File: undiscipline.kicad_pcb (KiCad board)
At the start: 2 copper layers, 243 parts, among them J1 Conn_01x04_Male, J2 AVR-ISP-6, J2 USB_B_Micro, SW1 SW_Push, SW10 SW_Push, SW11 SW_Push, SW12 SW_Push, SW13 SW_Push, SW14 SW_Push, SW15 SW_Push, SW16 SW_Push, SW17 SW_Push, SW18 SW_Push, SW19 SW_Push, SW2 SW_Push, SW20 SW_Push, SW21 SW_Push, SW22 SW_Push, SW23 SW_Push, SW24 SW_Push, SW25 SW_Push, SW26 SW_Push, SW27 SW_Push, SW28 SW_Push, SW29 SW_Push, SW3 SW_Push, SW30 SW_Push, SW31 SW_Push, SW32 SW_Push, SW33 SW_Push, SW34 SW_Push, SW35 SW_Push, SW36 SW_Push, SW37 SW_Push, SW38 SW_Push, SW39 SW_Push, SW4 SW_Push, SW40 SW_Push, SW41 SW_Push, SW42 SW_Push, SW43 SW_Push, SW44 SW_Push, SW45 SW_Push, SW46 SW_Push, SW47 SW_Push, SW48 SW_Push, SW49 SW_Push, SW5 SW_Push, SW50 SW_Push, SW51 SW_Push, SW52 SW_Push, SW53 SW_Push, SW54 SW_Push, SW55 SW_Push, SW56 SW_Push, SW57 SW_Push, SW58 SW_Push, SW59 SW_Push, SW6 SW_Push, SW60 SW_Push, SW61 SW_Push, SW62 SW_Push, SW63 SW_Push, SW64 SW_Push, SW65 SW_Push, SW66 SW_Push, SW67 SW_Push, SW68 SW_Push, SW69 SW_Push, SW7 SW_Push, SW70 SW_Push, SW71 SW_Push, SW72 SW_Push, SW73 SW_Push, SW74 SW_Push, SW75 SW_Push, SW8 SW_Push, SW9 SW_Push, U1 ATmega32A-PU, Y1 16MHz

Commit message: Add ws2812b footprint
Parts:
- moved REF** 0.18 mm to (52.2, 80.9)

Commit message: Add LEDs under each key
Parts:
- removed the REF** at (52.2, 80.9)
- added D100: WS2812B, LED_SMD:LED_WS2812B_PLCC4_5.0x5.0mm_P3.2mm, F.Cu at (80.5, 123.7)
- added D101: WS2812B, LED_SMD:LED_WS2812B_PLCC4_5.0x5.0mm_P3.2mm, F.Cu at (99.5, 123.7)
- added D102: WS2812B, LED_SMD:LED_WS2812B_PLCC4_5.0x5.0mm_P3.2mm, F.Cu at (118.5, 123.7)
- added D103: WS2812B, LED_SMD:LED_WS2812B_PLCC4_5.0x5.0mm_P3.2mm, F.Cu at (137.5, 123.7)
- added D104: WS2812B, LED_SMD:LED_WS2812B_PLCC4_5.0x5.0mm_P3.2mm, F.Cu at (156.5, 123.7)
- added D105: WS2812B, LED_SMD:LED_WS2812B_PLCC4_5.0x5.0mm_P3.2mm, F.Cu at (175.5, 123.7)
- added D106: WS2812B, LED_SMD:LED_WS2812B_PLCC4_5.0x5.0mm_P3.2mm, F.Cu at (194.5, 123.7)
- added D107: WS2812B, LED_SMD:LED_WS2812B_PLCC4_5.0x5.0mm_P3.2mm, F.Cu at (213.5, 123.7)
- added D108: WS2812B, LED_SMD:LED_WS2812B_PLCC4_5.0x5.0mm_P3.2mm, F.Cu at (232.5, 123.7)
- added D109: WS2812B, LED_SMD:LED_WS2812B_PLCC4_5.0x5.0mm_P3.2mm, F.Cu at (251.5, 123.7)
- added D110: WS2812B, LED_SMD:LED_WS2812B_PLCC4_5.0x5.0mm_P3.2mm, F.Cu at (270.5, 123.7)
- added D111: WS2812B, LED_SMD:LED_WS2812B_PLCC4_5.0x5.0mm_P3.2mm, F.Cu at (289.5, 123.7)
- added D112: WS2812B, LED_SMD:LED_WS2812B_PLCC4_5.0x5.0mm_P3.2mm, F.Cu at (313.2, 123.7)
- added D113: WS2812B, LED_SMD:LED_WS2812B_PLCC4_5.0x5.0mm_P3.2mm, F.Cu at (341.8, 123.7)
- added D114: WS2812B, LED_SMD:LED_WS2812B_PLCC4_5.0x5.0mm_P3.2mm, F.Cu at (360.8, 123.7)
- added D115: WS2812B, LED_SMD:LED_WS2812B_PLCC4_5.0x5.0mm_P3.2mm, F.Cu at (59.1, 142.7)
- added D116: WS2812B, LED_SMD:LED_WS2812B_PLCC4_5.0x5.0mm_P3.2mm, F.Cu at (85.2, 142.7)
- added D117: WS2812B, LED_SMD:LED_WS2812B_PLCC4_5.0x5.0mm_P3.2mm, F.Cu at (104.2, 142.7)
- added D118: WS2812B, LED_SMD:LED_WS2812B_PLCC4_5.0x5.0mm_P3.2mm, F.Cu at (123.2, 142.7)
- added D119: WS2812B, LED_SMD:LED_WS2812B_PLCC4_5.0x5.0mm_P3.2mm, F.Cu at (142.2, 142.7)
- added D120: WS2812B, LED_SMD:LED_WS2812B_PLCC4_5.0x5.0mm_P3.2mm, F.Cu at (161.2, 142.7)
- added D121: WS2812B, LED_SMD:LED_WS2812B_PLCC4_5.0x5.0mm_P3.2mm, F.Cu at (180.2, 142.7)
- added D122: WS2812B, LED_SMD:LED_WS2812B_PLCC4_5.0x5.0mm_P3.2mm, F.Cu at (199.2, 142.7)
- added D123: WS2812B, LED_SMD:LED_WS2812B_PLCC4_5.0x5.0mm_P3.2mm, F.Cu at (218.2, 142.7)
- added D124: WS2812B, LED_SMD:LED_WS2812B_PLCC4_5.0x5.0mm_P3.2mm, F.Cu at (237.2, 142.7)
- added D125: WS2812B, LED_SMD:LED_WS2812B_PLCC4_5.0x5.0mm_P3.2mm, F.Cu at (256.2, 142.7)
- added D126: WS2812B, LED_SMD:LED_WS2812B_PLCC4_5.0x5.0mm_P3.2mm, F.Cu at (275.2, 142.7)
- added D127: WS2812B, LED_SMD:LED_WS2812B_PLCC4_5.0x5.0mm_P3.2mm, F.Cu at (306.1, 142.7)
- added D128: WS2812B, LED_SMD:LED_WS2812B_PLCC4_5.0x5.0mm_P3.2mm, F.Cu at (341.8, 142.7)
- added D129: WS2812B, LED_SMD:LED_WS2812B_PLCC4_5.0x5.0mm_P3.2mm, F.Cu at (360.8, 142.7)
- added D130: WS2812B, LED_SMD:LED_WS2812B_PLCC4_5.0x5.0mm_P3.2mm, F.Cu at (63.9, 161.7)
- added D131: WS2812B, LED_SMD:LED_WS2812B_PLCC4_5.0x5.0mm_P3.2mm, F.Cu at (94.8, 161.7)
- added D132: WS2812B, LED_SMD:LED_WS2812B_PLCC4_5.0x5.0mm_P3.2mm, F.Cu at (113.8, 161.7)
- added D133: WS2812B, LED_SMD:LED_WS2812B_PLCC4_5.0x5.0mm_P3.2mm, F.Cu at (132.8, 161.7)
- added D134: WS2812B, LED_SMD:LED_WS2812B_PLCC4_5.0x5.0mm_P3.2mm, F.Cu at (151.8, 161.7)
- added D135: WS2812B, LED_SMD:LED_WS2812B_PLCC4_5.0x5.0mm_P3.2mm, F.Cu at (170.8, 161.7)
- added D136: WS2812B, LED_SMD:LED_WS2812B_PLCC4_5.0x5.0mm_P3.2mm, F.Cu at (189.8, 161.7)
- added D137: WS2812B, LED_SMD:LED_WS2812B_PLCC4_5.0x5.0mm_P3.2mm, F.Cu at (208.8, 161.7)
- added D138: WS2812B, LED_SMD:LED_WS2812B_PLCC4_5.0x5.0mm_P3.2mm, F.Cu at (227.8, 161.7)
- added D139: WS2812B, LED_SMD:LED_WS2812B_PLCC4_5.0x5.0mm_P3.2mm, F.Cu at (246.8, 161.7)
- added D140: WS2812B, LED_SMD:LED_WS2812B_PLCC4_5.0x5.0mm_P3.2mm, F.Cu at (265.8, 161.7)
- added D141: WS2812B, LED_SMD:LED_WS2812B_PLCC4_5.0x5.0mm_P3.2mm, F.Cu at (301.4, 161.7)
- added D142: WS2812B, LED_SMD:LED_WS2812B_PLCC4_5.0x5.0mm_P3.2mm, F.Cu at (341.8, 166.4)
- added D143: WS2812B, LED_SMD:LED_WS2812B_PLCC4_5.0x5.0mm_P3.2mm, F.Cu at (54.4, 180.7)
- added D144: WS2812B, LED_SMD:LED_WS2812B_PLCC4_5.0x5.0mm_P3.2mm, F.Cu at (78.1, 180.7)
- added D145: WS2812B, LED_SMD:LED_WS2812B_PLCC4_5.0x5.0mm_P3.2mm, F.Cu at (101.9, 180.7)
- added D146: WS2812B, LED_SMD:LED_WS2812B_PLCC4_5.0x5.0mm_P3.2mm, F.Cu at (125.6, 180.7)
- added D147: WS2812B, LED_SMD:LED_WS2812B_PLCC4_5.0x5.0mm_P3.2mm, F.Cu at (196.9, 180.7)
- added D148: WS2812B, LED_SMD:LED_WS2812B_PLCC4_5.0x5.0mm_P3.2mm, F.Cu at (268.1, 180.7)
- added D149: WS2812B, LED_SMD:LED_WS2812B_PLCC4_5.0x5.0mm_P3.2mm, F.Cu at (291.9, 180.7)
- added D150: WS2812B, LED_SMD:LED_WS2812B_PLCC4_5.0x5.0mm_P3.2mm, F.Cu at (322.8, 185.4)
- added D151: WS2812B, LED_SMD:LED_WS2812B_PLCC4_5.0x5.0mm_P3.2mm, F.Cu at (341.8, 185.4)
- added D152: WS2812B, LED_SMD:LED_WS2812B_PLCC4_5.0x5.0mm_P3.2mm, F.Cu at (360.8, 185.4)
- added D78: WS2812B, LED_SMD:LED_WS2812B_PLCC4_5.0x5.0mm_P3.2mm, F.Cu at (52.0, 81.0)
- added D79: WS2812B, LED_SMD:LED_WS2812B_PLCC4_5.0x5.0mm_P3.2mm, F.Cu at (80.5, 81.0)
- added D80: WS2812B, LED_SMD:LED_WS2812B_PLCC4_5.0x5.0mm_P3.2mm, F.Cu at (99.5, 81.0)
- added D81: WS2812B, LED_SMD:LED_WS2812B_PLCC4_5.0x5.0mm_P3.2mm, F.Cu at (118.5, 81.0)
- added D82: WS2812B, LED_SMD:LED_WS2812B_PLCC4_5.0x5.0mm_P3.2mm, F.Cu at (137.5, 81.0)
- added D83: WS2812B, LED_SMD:LED_WS2812B_PLCC4_5.0x5.0mm_P3.2mm, F.Cu at (52.0, 104.7)
- added D84: WS2812B, LED_SMD:LED_WS2812B_PLCC4_5.0x5.0mm_P3.2mm, F.Cu at (71.0, 104.7)
- added D85: WS2812B, LED_SMD:LED_WS2812B_PLCC4_5.0x5.0mm_P3.2mm, F.Cu at (90.0, 104.7)
- added D86: WS2812B, LED_SMD:LED_WS2812B_PLCC4_5.0x5.0mm_P3.2mm, F.Cu at (109.0, 104.7)
- added D87: WS2812B, LED_SMD:LED_WS2812B_PLCC4_5.0x5.0mm_P3.2mm, F.Cu at (128.0, 104.7)
- added D88: WS2812B, LED_SMD:LED_WS2812B_PLCC4_5.0x5.0mm_P3.2mm, F.Cu at (147.0, 104.7)
- added D89: WS2812B, LED_SMD:LED_WS2812B_PLCC4_5.0x5.0mm_P3.2mm, F.Cu at (166.0, 104.7)
- added D90: WS2812B, LED_SMD:LED_WS2812B_PLCC4_5.0x5.0mm_P3.2mm, F.Cu at (185.0, 104.7)
- added D91: WS2812B, LED_SMD:LED_WS2812B_PLCC4_5.0x5.0mm_P3.2mm, F.Cu at (204.0, 104.7)
- added D92: WS2812B, LED_SMD:LED_WS2812B_PLCC4_5.0x5.0mm_P3.2mm, F.Cu at (223.0, 104.7)
- added D93: WS2812B, LED_SMD:LED_WS2812B_PLCC4_5.0x5.0mm_P3.2mm, F.Cu at (242.0, 104.7)
- added D94: WS2812B, LED_SMD:LED_WS2812B_PLCC4_5.0x5.0mm_P3.2mm, F.Cu at (261.0, 104.7)
- added D95: WS2812B, LED_SMD:LED_WS2812B_PLCC4_5.0x5.0mm_P3.2mm, F.Cu at (280.0, 104.7)
- added D96: WS2812B, LED_SMD:LED_WS2812B_PLCC4_5.0x5.0mm_P3.2mm, F.Cu at (308.5, 104.7)
- added D97: WS2812B, LED_SMD:LED_WS2812B_PLCC4_5.0x5.0mm_P3.2mm, F.Cu at (341.8, 104.7)
- added D98: WS2812B, LED_SMD:LED_WS2812B_PLCC4_5.0x5.0mm_P3.2mm, F.Cu at (360.8, 104.7)
- added D99: WS2812B, LED_SMD:LED_WS2812B_PLCC4_5.0x5.0mm_P3.2mm, F.Cu at (56.8, 123.7)
- moved D70 16.5 mm to (194.7, 165.4), turned to 180 degrees
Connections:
- U1 pad 19: Net-(U1-Pad19) -> LED
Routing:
- net row1: track 308.8 -> 0.00 mm
- net row5: track 308.3 -> 0.00 mm
- net row2: track 304.0 -> 0.00 mm
- net row3: track 301.6 -> 0.00 mm
- net row4: track 279.8 -> 0.00 mm
- net col11: track 105.9 -> 0.00 mm
- net col1: track 100.3 -> 0.00 mm
- net col13: track 96.5 -> 0.00 mm
- net col3: track 93.7 -> 0.00 mm
- net col4: track 91.7 -> 0.00 mm
- net col7: track 91.5 -> 0.00 mm
- net col0: track 90.6 -> 0.00 mm
- net col15: track 81.4 -> 0.00 mm
- net col14: track 80.7 -> 0.00 mm
- net col9: track 70.2 -> 0.00 mm
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
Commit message: WIP
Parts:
- removed the J2 at (260.2, 71.8)
- added REF**: MountingHole_2.2mm_M2, MountingHole:MountingHole_2.2mm_M2, F.Cu at (371.8, 189.8)
- added REF**: MountingHole_2.2mm_M2, MountingHole:MountingHole_2.2mm_M2, F.Cu at (96.9, 107.6)
- added REF**: MountingHole_2.2mm_M2, MountingHole:MountingHole_2.2mm_M2, F.Cu at (157.5, 63.2)
- added REF**: MountingHole_2.2mm_M2, MountingHole:MountingHole_2.2mm_M2, F.Cu at (157.5, 86.1)
- added REF**: MountingHole_2.2mm_M2, MountingHole:MountingHole_2.2mm_M2, F.Cu at (371.8, 63.2)
- added REF**: MountingHole_2.2mm_M2, MountingHole:MountingHole_2.2mm_M2, F.Cu at (371.8, 86.1)
- added REF**: MountingHole_2.2mm_M2, MountingHole:MountingHole_2.2mm_M2, F.Cu at (41.0, 86.1)
- added REF**: MountingHole_2.2mm_M2, MountingHole:MountingHole_2.2mm_M2, F.Cu at (41.0, 63.2)
- added REF**: MountingHole_2.2mm_M2, MountingHole:MountingHole_2.2mm_M2, F.Cu at (41.0, 189.8)
- added REF**: MountingHole_2.2mm_M2, MountingHole:MountingHole_2.2mm_M2, F.Cu at (251.5, 86.1)
- added REF**: MountingHole_2.2mm_M2, MountingHole:MountingHole_2.2mm_M2, F.Cu at (251.5, 63.0)
- added REF**: MountingHole_2.2mm_M2, MountingHole:MountingHole_2.2mm_M2, F.Cu at (310.9, 164.5)
- added REF**: MountingHole_2.2mm_M2, MountingHole:MountingHole_2.2mm_M2, F.Cu at (209.0, 168.0)
- added REF**: MountingHole_2.2mm_M2, MountingHole:MountingHole_2.2mm_M2, F.Cu at (73.4, 164.5)
- added REF**: MountingHole_2.2mm_M2, MountingHole:MountingHole_2.2mm_M2, F.Cu at (315.4, 107.6)
- added REF**: MountingHole_2.2mm_M2, MountingHole:MountingHole_2.2mm_M2, F.Cu at (210.9, 107.6)
- D1, D10, D11, D12, D13, D14, D15, D16, D17, D18, D19, D2, D20, D21, D22, D23, D24, D25, D26, D27, D28, D29, D3, D30, D31, D32, D33, D34, D35, D36, D37, D38, D39, D4, D40, D41, D42, D43, D44, D45, D46, D47, D48, D49, D5, D50, D51, D52, D53, D54, D55, D56, D57, D58, D59, D6, D60, D61, D62, D63, D64, D65, D66, D67, D68, D69, D7, D70, D71, D72, D73, D74, D75, D8, D9: moved to B.Cu
- J1: footprint Connector_PinHeader_1.00mm:PinHeader_1x04_P1.00mm_Vertical -> Connector_PinHeader_2.54mm:PinHeader_1x04_P2.54mm_Vertical
- Y1: footprint Crystal:Crystal_HC18-U_Vertical -> Crystal:Crystal_HC49-4H_Vertical
- moved J1 64.3 mm to (177.6, 84.7), turned to 90 degrees
- moved D2 60.2 mm to (72.3, 81.2)
- moved D3 54.7 mm to (91.3, 81.2)
- moved D4 52.0 mm to (110.3, 81.2)
- moved D5 49.7 mm to (129.3, 81.2)
- moved SW_BOOT1 32.3 mm to (278.2, 61.8)
- moved SW_RESET1 32.3 mm to (266.5, 61.8)
- moved J2 22.3 mm to (295.0, 59.8)
- moved D76 17.3 mm to (310.4, 79.8)
- moved D77 17.3 mm to (306.2, 79.8)
- moved C3 17.3 mm to (308.3, 73.8)
- moved D70 16.7 mm to (188.7, 181.0), turned to 90 degrees
- moved D1 16.1 mm to (43.8, 81.2), turned to 90 degrees
- moved R1 5.83 mm to (310.8, 70.3)
- moved R3 5.83 mm to (305.8, 64.5)
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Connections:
- J1 pad 1: SDA -> GND
- J1 pad 2: SCL -> +5V
- J1 pad 3: GND -> SCL
- J1 pad 4: +5V -> SDA
- SW53 pad 2: col1 -> col0
- SW71 pad 2: Net-(SW71-Pad2) -> col10
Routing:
- net row1: track 0.00 -> 368.9 mm
- net row2: track 0.00 -> 364.2 mm
- net row3: track 0.00 -> 357.8 mm
- net row5: track 0.00 -> 343.2 mm
- net row4: track 0.00 -> 326.8 mm
- net col1: track 0.00 -> 116.4 mm
- net col0: track 0.00 -> 111.1 mm
- net col10: track 0.00 -> 108.7 mm
- net col11: track 0.00 -> 106.2 mm
- net row0: track 0.00 -> 101.5 mm
- net col13: track 0.00 -> 98.3 mm
- net col4: track 0.00 -> 98.1 mm
- net col3: track 0.00 -> 98.1 mm
- net col2: track 0.00 -> 96.2 mm
- net col15: track 0.00 -> 80.7 mm
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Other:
- board outline added: 337.8 x 133.5 mm
- board text added: "UNDISCIPLINE"

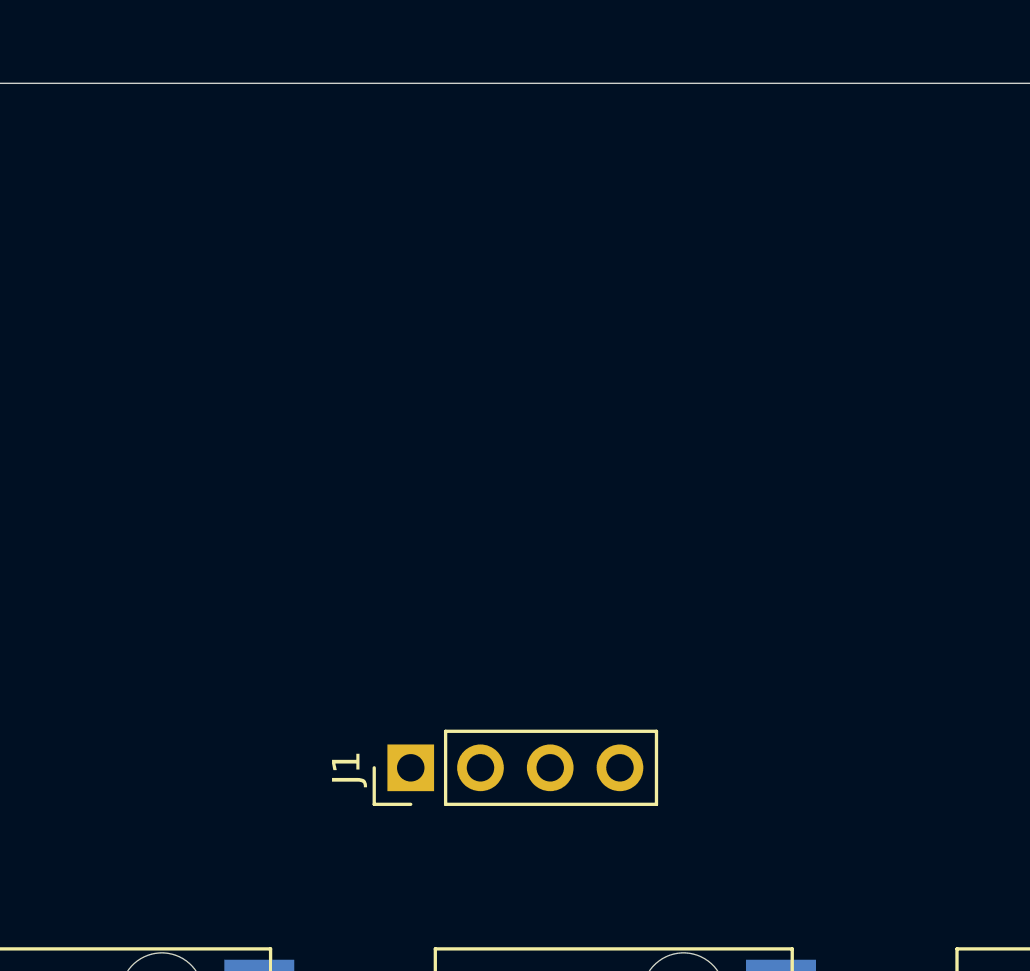
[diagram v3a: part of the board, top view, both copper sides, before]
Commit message: Add 3d models
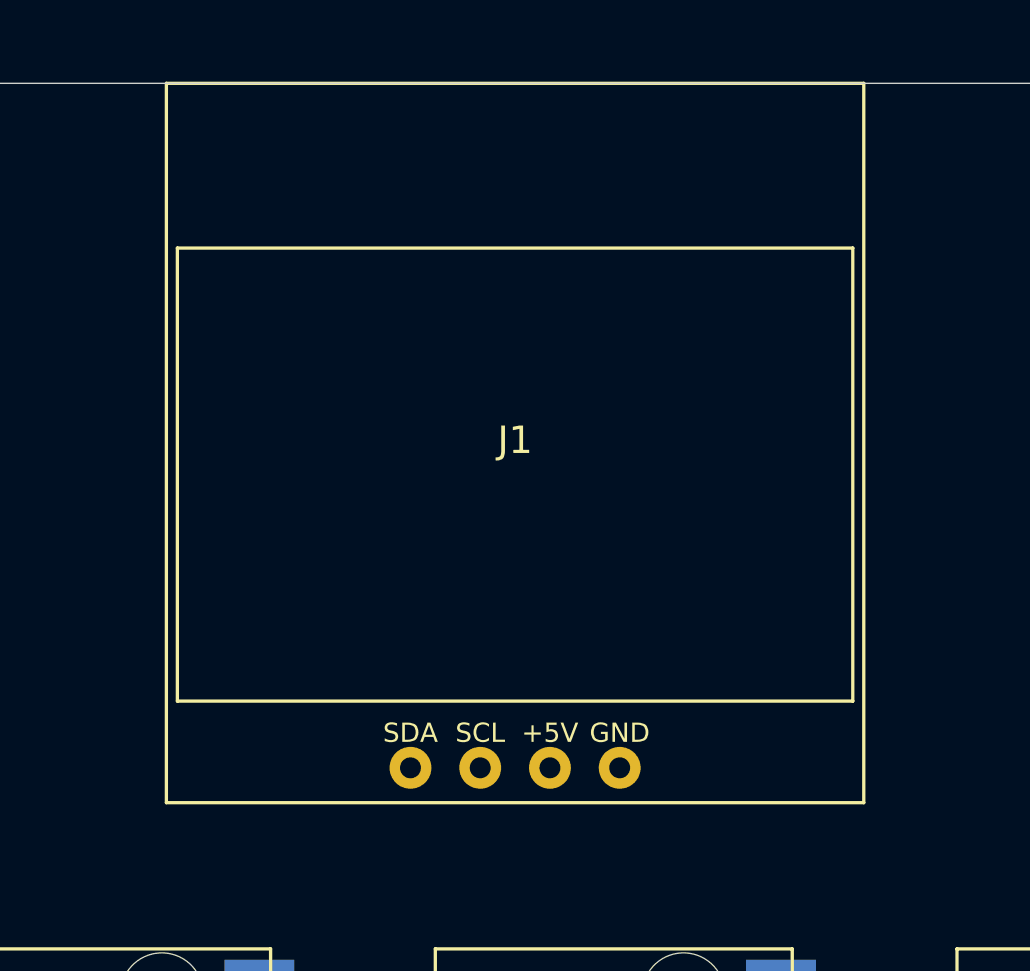
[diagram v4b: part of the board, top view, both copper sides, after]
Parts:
- J1: footprint Connector_PinHeader_2.54mm:PinHeader_1x04_P2.54mm_Vertical -> undiscipline:OLED128x64
- moved J1 12.0 mm to (181.4, 73.2), turned to 180 degrees

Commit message: Add more tracks for LEDs
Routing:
- net Net-(D129-Pad2): track 0.00 -> 60.0 mm, vias 0 -> 2
- net Net-(D115-Pad4): track 0.00 -> 48.4 mm, vias 0 -> 2
- net Net-(D141-Pad4): track 0.00 -> 41.7 mm
- net Net-(D78-Pad2): track 0.00 -> 40.2 mm, vias 0 -> 2
- net Net-(D83-Pad2): track 0.00 -> 36.4 mm
- net Net-(D140-Pad4): track 0.00 -> 35.0 mm
- net Net-(D127-Pad2): track 0.00 -> 35.0 mm
- net Net-(D114-Pad4): track 0.00 -> 33.9 mm, vias 0 -> 2
- net Net-(D96-Pad2): track 0.00 -> 30.8 mm
- net Net-(D126-Pad2): track 0.00 -> 30.2 mm
- net Net-(D78-Pad4): track 0.00 -> 27.7 mm
- net Net-(D95-Pad2): track 0.00 -> 27.7 mm
- net Net-(D112-Pad4): track 0.00 -> 27.7 mm
- net Net-(D115-Pad2): track 0.00 -> 25.3 mm
- net Net-(D100-Pad2): track 0.00 -> 22.9 mm
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- added copper zone on B.Cu, net GND
- added copper zone on F.Cu, net GND

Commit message: More tracks...
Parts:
- moved C4 1.55 mm to (330.2, 83.8)
- moved C1 1.27 mm to (353.5, 86.1)
- moved C2 1.27 mm to (338.5, 86.1)
- moved Y1 1.27 mm to (348.5, 85.1)
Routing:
- net +5V: track 0.00 -> 233.5 mm, vias 0 -> 50
- net col0: track 111.1 -> 211.4 mm
- net boot: track 0.00 -> 89.9 mm
- net reset: track 0.00 -> 78.8 mm
- net col1: track 116.4 -> 188.2 mm
- net Net-(D146-Pad2): track 0.00 -> 70.6 mm
- net Net-(D147-Pad2): track 0.00 -> 70.6 mm
- net col2: track 96.2 -> 148.9 mm
- net Net-(D130-Pad2): track 0.00 -> 52.4 mm, vias 0 -> 2
- net D-: track 0.00 -> 51.4 mm
- net D+: track 0.00 -> 47.7 mm
- net col3: track 98.1 -> 131.6 mm
- net Net-(D149-Pad2): track 0.00 -> 32.2 mm
- net Net-(D130-Pad4): track 0.00 -> 30.2 mm
- net Net-(D76-Pad1): track 0.00 -> 23.7 mm
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- added copper zone on In1.Cu, net +5V
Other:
- copper layers 2 -> 4

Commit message: Finish routing tracks
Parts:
- added J3: Conn_01x02_Male, Connector_PinHeader_2.54mm:PinHeader_1x02_P2.54mm_Horizontal, B.Cu at (246.4, 74.2)
- added J4: Conn_01x02_Male, Connector_PinHeader_2.54mm:PinHeader_1x02_P2.54mm_Horizontal, B.Cu at (371.9, 70.1)
- C5: moved to B.Cu
- moved D76 31.8 mm to (279.7, 71.6), turned to 180 degrees
- moved D77 27.0 mm to (279.7, 75.2), turned to 180 degrees
- moved SW_BOOT1 7.40 mm to (271.1, 63.8)
- moved SW_RESET1 7.40 mm to (259.4, 63.8)
- moved C3 6.35 mm to (301.9, 73.8)
- moved J2 6.35 mm to (288.6, 59.8)
- moved R3 6.35 mm to (299.4, 64.5)
- moved R1 6.35 mm to (304.5, 70.3)
- moved R2 6.35 mm to (304.5, 67.4)
- moved C4 4.83 mm to (335.0, 83.6), turned to 225 degrees
- moved C5 1.40 mm to (341.9, 61.7), turned to 0 degrees
- moved C1 0.32 mm to (353.8, 86.1)
- moved REF** 0.23 mm to (251.5, 63.2)
- moved Y1 0.21 mm to (348.5, 84.9)
- moved C2 0.18 mm to (338.3, 86.1)
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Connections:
- J1 pad 3: SCL -> Net-(J1-Pad3)
- J1 pad 4: SDA -> Net-(J1-Pad4)
- U1 pad 1: col0 -> col4
- U1 pad 14: col14 -> col12
- U1 pad 15: col15 -> col13
- U1 pad 19: LED -> col14
- U1 pad 2: col1 -> col5
- U1 pad 20: Net-(U1-Pad20) -> col15
- U1 pad 24: col8 -> col3
- U1 pad 25: col9 -> col2
- U1 pad 26: col10 -> col1
- U1 pad 27: col11 -> col0
- U1 pad 28: col12 -> Net-(U1-Pad28)
- U1 pad 29: col13 -> Net-(U1-Pad29)
- U1 pad 3: col2 -> col6
- U1 pad 34: Net-(U1-Pad34) -> row5
- U1 pad 35: row5 -> row4
- U1 pad 36: row4 -> row3
- U1 pad 37: row3 -> row2
- U1 pad 38: row2 -> row1
- U1 pad 39: row1 -> row0
- U1 pad 4: col3 -> col7
- U1 pad 40: row0 -> LED
- U1 pad 5: col4 -> col8
- U1 pad 6: col5 -> col9
- U1 pad 7: col6 -> col10
- U1 pad 8: col7 -> col11
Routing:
- net +5V: track 233.5 -> 509.6 mm, vias 50 -> 76
- net col3: track 131.6 -> 383.3 mm
- net col2: track 148.9 -> 361.4 mm
- net col1: track 188.2 -> 398.1 mm
- net col0: track 211.4 -> 418.7 mm
- net row0: track 101.5 -> 308.1 mm, vias 0 -> 2
- net col4: track 111.4 -> 309.0 mm
- net LED: track 0.00 -> 190.0 mm, vias 0 -> 1
- net col5: track 70.4 -> 243.1 mm
- net row4: track 326.8 -> 488.3 mm, vias 0 -> 1
- net col7: track 70.4 -> 230.8 mm
- net row5: track 343.2 -> 502.8 mm
- net col6: track 70.4 -> 226.4 mm
- net row3: track 357.8 -> 483.1 mm
- net col8: track 68.5 -> 190.5 mm
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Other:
- net class Default: clearance 0.2 -> 0.5; trace_width 0.25 -> 0.5; via_dia 0.8 -> 1.6; via_drill 0.4 -> 0.8
- rule trace_clearance: 0.2 -> 0.5
- rule trace_min: 0.2 -> 0.5
- rule via_min_size: 0.4 -> 1.6

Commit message: Add mounting holes; move some tracks
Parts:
- removed the REF** at (371.8, 189.8)
- removed the REF** at (157.5, 63.2)
- removed the REF** at (157.5, 86.1)
- removed the REF** at (371.8, 63.2)
- removed the REF** at (371.8, 86.1)
- removed the REF** at (41.0, 86.1)
- removed the REF** at (41.0, 63.2)
- removed the REF** at (41.0, 189.8)
- removed the REF** at (209.0, 168.0)
- added H1: MountingHole_Pad, MountingHole:MountingHole_2.2mm_M2_DIN965_Pad_TopBottom, F.Cu at (41.0, 189.8)
- added H2: MountingHole_Pad, MountingHole:MountingHole_2.2mm_M2_DIN965_Pad_TopBottom, F.Cu at (41.0, 63.2)
- added H3: MountingHole_Pad, MountingHole:MountingHole_2.2mm_M2_DIN965_Pad_TopBottom, F.Cu at (157.5, 63.2)
- added H4: MountingHole_Pad, MountingHole:MountingHole_2.2mm_M2_DIN965_Pad_TopBottom, F.Cu at (41.0, 86.1)
- added H5: MountingHole_Pad, MountingHole:MountingHole_2.2mm_M2_DIN965_Pad_TopBottom, F.Cu at (371.8, 63.2)
- added H6: MountingHole_Pad, MountingHole:MountingHole_2.2mm_M2_DIN965_Pad_TopBottom, F.Cu at (371.8, 86.1)
- added H7: MountingHole_Pad, MountingHole:MountingHole_2.2mm_M2_DIN965_Pad_TopBottom, F.Cu at (157.5, 86.1)
- added H8: MountingHole_Pad, MountingHole:MountingHole_2.2mm_M2_DIN965_Pad_TopBottom, F.Cu at (371.8, 189.8)
- added H9: MountingHole_Pad, MountingHole:MountingHole_2.2mm_M2_DIN965_Pad_TopBottom, F.Cu at (209.0, 168.0)
- moved J4 2.97 mm to (369.1, 71.1)
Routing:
- net SCL: track 19.6 -> 12.2 mm
- net row0: track 308.1 -> 303.1 mm
- net Net-(D115-Pad4): track 29.7 -> 34.6 mm
- net Net-(D91-Pad2): track 20.5 -> 15.5 mm
- net Net-(D130-Pad2): track 41.2 -> 45.3 mm
- net LED: track 190.0 -> 186.1 mm
- net Net-(D125-Pad2): track 18.3 -> 15.5 mm
- net Net-(D126-Pad2): track 30.2 -> 27.4 mm
- net Net-(D124-Pad2): track 18.3 -> 15.5 mm
- net Net-(D123-Pad2): track 18.3 -> 15.5 mm
- net Net-(D122-Pad2): track 18.3 -> 15.5 mm
- net Net-(D121-Pad2): track 18.3 -> 15.5 mm
- net Net-(D120-Pad2): track 18.3 -> 15.5 mm
- net Net-(D119-Pad2): track 18.3 -> 15.5 mm
- net Net-(D118-Pad2): track 18.3 -> 15.5 mm
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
